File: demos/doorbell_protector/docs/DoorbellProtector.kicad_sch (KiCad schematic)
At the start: 15 parts

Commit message: export: kicad_sch — Phase 2.5b: layered placement, wire routing, KiCad 10 compatibility (#23)
* export: kicad_sch — Phase 2.5b: layered placement + routing + KiCad 9 fix

Placement (placement.py, complete rewrite):
- Replaces naive grid with Layered Signal Flow algorithm (spec §5 stages 1–8)
- Stage 1: band classification — power chips/rails at top, LEDs at bottom,
  everything else in the signal band
- Stage 2: signal-flow DAG via BFS from Rail/Connector sources; layer = BFS
  distance from nearest source
- Stage 3–4: place within (band, layer) cells at 1500-mil (38.1 mm) same-band
  spacing, 1000-mil inter-band gutter, 25.4 mm page margin
- Stage 6: cluster breakup — up to 10 iterations shifting same-band parts
  that land closer than 0.9× SAME_BAND_SPACING_MM
- Stage 8: page sized to fit (A4 → A3 → A2 → A1)
- grid_place() and sheet_size_mm() kept as shims for backward-compat

Routing (routing.py, new file):
- route_net(): connects stub ends with Manhattan L-shapes (horizontal first)
- find_junctions(): returns points where ≥3 wire endpoints coincide
- renderer uses routed wires between signal-net stub ends

Hierarchical (hierarchical.py, new file):
- collect_boards(), is_multi_board(), sub_sheet_filename() — interface stub
  for multi-Board sub-sheet emission (full implementation deferred)

KiCad 9 sub-symbol name fix (library_loader.py):
- KiCad 9 schematics expect sub-symbols nested inside their parent in
  lib_symbols to use the bare name (R_0_1, LED_0_1, 4069_1_0) — NOT the
  lib-qualified name (Device:R_0_1, Device:LED_0_1, 4xxx:4069_1_0)
- Fixed _qualify_names() to add the lib: prefix only to the exact parent
  symbol name using a lookahead (?=") that prevents sub-unit names from
  being qualified

Tests (+25 tests):
- test_placement.py: band classification, all-on-grid, determinism,
  minimum spacing, power < signal < indicator Y ordering, page sizing
- test_routing.py: H/V segments, L-shapes, orthogonality, grid snap,
  junction detection

Golden files re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
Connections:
- net Net-(Q2-b) is gone; now on net Net-(C4-t1): R4.1, R4.2
- net Net-(Q2-c) is gone; now on net Net-(C4-t1): R5.1, R5.2
- net Net-(C4-t1): now also C5.1, C5.2, R2.1, R2.2, R3.1, R3.2, R6.1, R6.2, R7.1, R7.2, R8.1, R8.2
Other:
- moved on the sheet: C1, C2, C3, C4, C5, D1, D2, R1, R2, R3, R4, R5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

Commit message: framework: passive + diode terminals mandatory (#30)
Continuation of the LED.cathode regression fix (#29). Resistor,
Capacitor, Inductor, and every Diode subclass had their terminals
declared `mandatory=False` with the same "structurally inert under
graph evaluation" justification — letting demos declare BOM-only
timing / decoupling / pull-up parts without wiring them, then ship
breadboard SVGs and netlists where those parts sat orphaned.

A real resistor / capacitor / inductor / diode with a dangling
terminal does nothing. Marking the ports mandatory closes the
silent regression at the framework layer.

  - `src/components/passives/{resistor,capacitor,inductor}.py` and
    every diode subclass under `src/components/diodes/` now declare
    their terminals `mandatory=True`.
  - `tests/components/test_{resistor,capacitor,inductor}.py`:
    regression tests pin the new contract per component.
  - `tests/components/test_diode_mandatory_terminals.py` (new):
    parametrized over D1N4001 / D1N4007 / D1N4148 / D1N4728A /
    D1N4733A / D1N4742A / D1N5817.
  - Six demos (`backup_power`, `bldc_motor`, `dice`,
    `doorbell_protector`, `fan_cooling`, `isolated_rs232`) had
    declared-but-unwired passives — each now wires them either to
    their datasheet-correct net (e.g. DoorbellProtector's flyback
    diode anode joins the relay coil_minus net) or as an isolated
    0-Ω passthrough with `dynamically_driven=True` where the part
    is genuinely BOM-only and the voltage-only simulator can't
    honour its behaviour. Comments at each call site explain
    which kind.
  - Test fixtures across CLI, refdes, format-roundtrip, kicad
    import, and per-format renderer tests updated so they still
    pin down the specific error each one exists to catch without
    tripping the new mandatory-pin check first.
  - All demo docs regenerated; goldens refreshed.

After this commit the breadboard SVGs show every BOM part connected
to something — no more orphaned caps and resistors float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
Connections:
- net Net-(C4-t1) is gone; now on net VCC: C4.1, C4.2, C5.1, C5.2, D2.1 (K), R1.1, R1.2, R2.1, R2.2, R3.1, R3.2, R4.1, R4.2, R5.1, R5.2, R6.1, R6.2, R7.1, R7.2, R8.1, R8.2
- net VCC: now also C1.1, C1.2, C2.1, C2.2, C3.1, C3.2

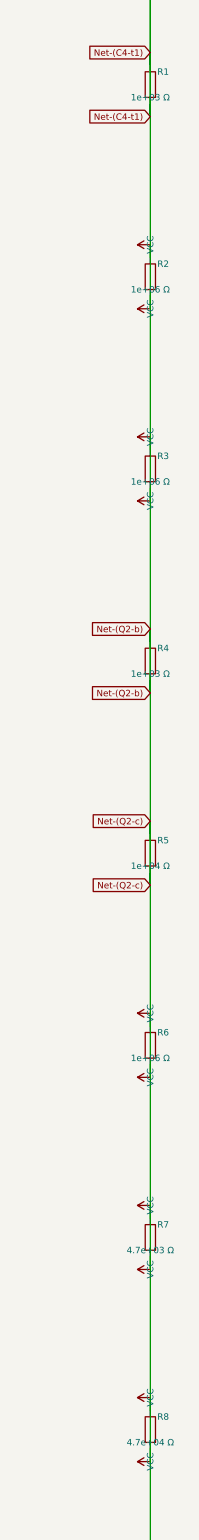
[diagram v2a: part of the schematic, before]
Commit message: units: Ohms.__str__ uses engineering notation (kΩ, MΩ, GΩ)
The previous `Ohms.__str__` formatted with bare `:.3g`, producing
unreadable scientific output for clean kilo / mega multiples:

  str(Ohms(10_000))     == "1e+04 Ω"      → now "10 kΩ"
  str(Ohms(100_000))    == "1e+05 Ω"      → now "100 kΩ"
  str(Ohms(1_000_000))  == "1e+06 Ω"      → now "1 MΩ"

The breadboard SVG visualiser surfaced the problem: a resistor body
labelled "100000Ω" makes a reader count zeros, while a label of
"100 kΩ" reads at a glance — exactly the convention every schematic
and parts catalogue uses. Centralising the engineering notation in
`Ohms.__str__` means every downstream consumer (assembly guide,
breadboard SVG, kicad netlist, BOM, reports) inherits the readable
form without each format adapter rolling its own formatter.

  - `Ohms.__str__` returns "47 Ω", "4.7 kΩ", "10 kΩ", "100 kΩ",
    "1 MΩ", "10 MΩ", "1 GΩ" per the kilo / mega / giga thresholds.
  - `Resistor.__str__` delegates to `str(self._ohms)` so it
    inherits the new notation (was producing the noisy "47.0 Ω"
    via raw float).
  - The breadboard visualiser's resistor body label uses
    `str(part.ohms)` directly (previously had a private
    `_format_ohms_compact` helper; removed).
  - `tests/components/test_resistor.py::test_str` updated for
    "47 Ω" (was "47.0 Ω"); new `test_str_renders_in_engineering_notation`
    pins kΩ / MΩ output across the kilo and mega thresholds.
  - All demo docs / goldens refreshed where the Ohms.__str__
    change affected the rendered output (breadboard SVGs, kicad
    sch value fields, BOM rows).
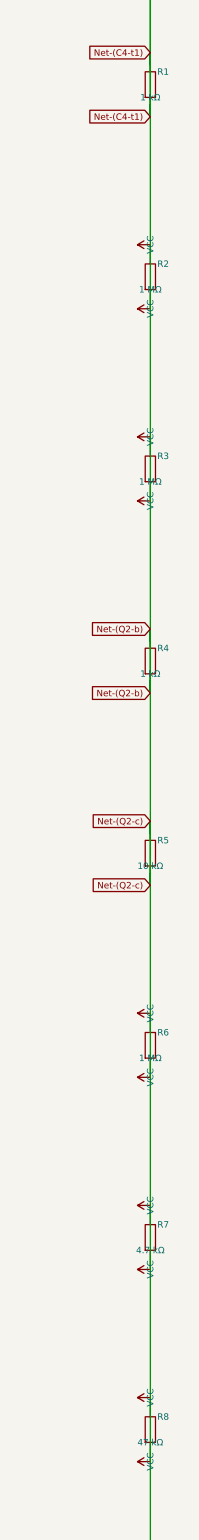
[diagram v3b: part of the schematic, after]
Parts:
- R1, R4: value 1e+03 Ω -> 1 kΩ
- R2, R3, R6: value 1e+06 Ω -> 1 MΩ
- R5: value 1e+04 Ω -> 10 kΩ
- R7: value 4.7e+03 Ω -> 4.7 kΩ
- R8: value 4.7e+04 Ω -> 47 kΩ
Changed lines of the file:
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@@
       (effects (font (size 1.27 1.27)))
     )
-    (property "Value" "1e+03 Ω"
+    (property "Value" "1 kΩ"
       (at 63.5 485.14 0)
       (effects (font (size 1.27 1.27)))
@@
       (effects (font (size 1.27 1.27)))
     )
-    (property "Value" "1e+06 Ω"
+    (property "Value" "1 MΩ"
       (at 63.5 523.24 0)
       (effects (font (size 1.27 1.27)))
@@
       (effects (font (size 1.27 1.27)))
     )
-    (property "Value" "1e+06 Ω"
+    (property "Value" "1 MΩ"
       (at 63.5 561.34 0)
       (effects (font (size 1.27 1.27)))
@@
       (effects (font (size 1.27 1.27)))
     )
-    (property "Value" "1e+03 Ω"
+    (property "Value" "1 kΩ"
       (at 63.5 599.44 0)
       (effects (font (size 1.27 1.27)))
@@
       (effects (font (size 1.27 1.27)))
     )
-    (property "Value" "1e+04 Ω"
+    (property "Value" "10 kΩ"
       (at 63.5 637.54 0)
       (effects (font (size 1.27 1.27)))
@@
       (effects (font (size 1.27 1.27)))
     )
-    (property "Value" "1e+06 Ω"
+    (property "Value" "1 MΩ"
       (at 63.5 675.64 0)
       (effects (font (size 1.27 1.27)))
@@
       (effects (font (size 1.27 1.27)))
     )
-    (property "Value" "4.7e+03 Ω"
+    (property "Value" "4.7 kΩ"
       (at 63.5 713.74 0)
       (effects (font (size 1.27 1.27)))
@@
       (effects (font (size 1.27 1.27)))
     )
-    (property "Value" "4.7e+04 Ω"
+    (property "Value" "47 kΩ"
       (at 63.5 751.84 0)
       (effects (font (size 1.27 1.27)))

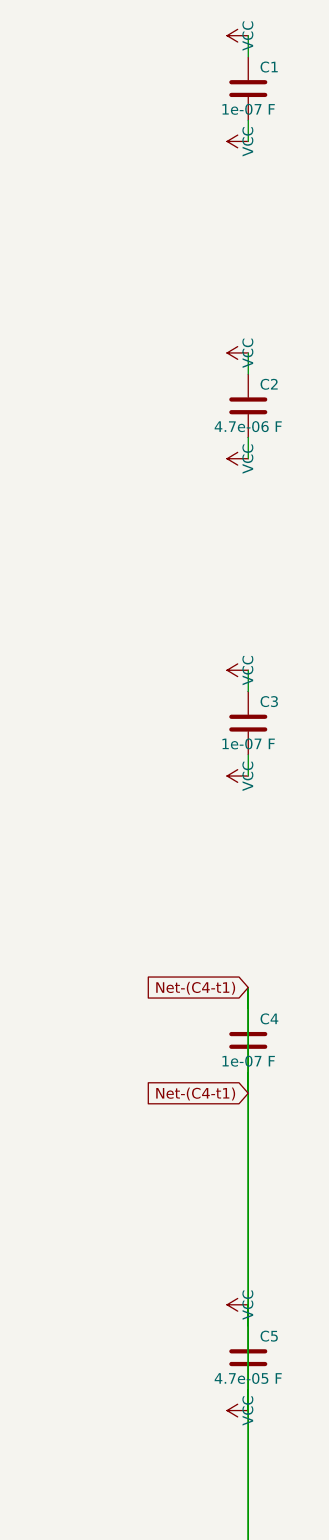
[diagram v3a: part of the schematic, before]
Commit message: units: Farads + Henries __str__ also use engineering notation
Same treatment as `Ohms.__str__` (previous commit) for the other two
passive engineering quantities. Demos contain caps and inductors
with values that the bare `:.3g` formatter would emit in scientific
form (`1e-07 F` for a 100 nF decoupling cap); centralising the
engineering notation on the unit class means every consumer
(reports, BOM, breadboard SVG, etc.) inherits the readable form.

  - `Farads.__str__` returns `100 pF`, `22 nF`, `100 nF`, `1 µF`,
    `4.7 µF`, `470 µF`, `1 mF`, `1 F` across the standard
    capacitance bands.
  - `Henries.__str__` returns `100 nH`, `10 µH`, `22 mH`, `1 H`
    across the standard inductance bands.
  - `Capacitor.__str__` and `Inductor.__str__` delegate to the
    unit class's str (were rolling raw-float formatters).
  - `framework.export.reports_common.part_description` now uses
    `str(part.ohms / farads / henries)` directly instead of the
    parallel `_format_ohms` / `_format_farads` / `_format_henries`
    helpers (removed — they duplicated the new logic on raw
    floats).
  - Breadboard SVG renderer now also labels capacitor and inductor
    bodies with their engineering-notation value (was only
    resistors).
  - `tests/framework/test_units.py`: parametrised regression tests
    for both unit classes across every band.
  - All affected demo docs / goldens refreshed.
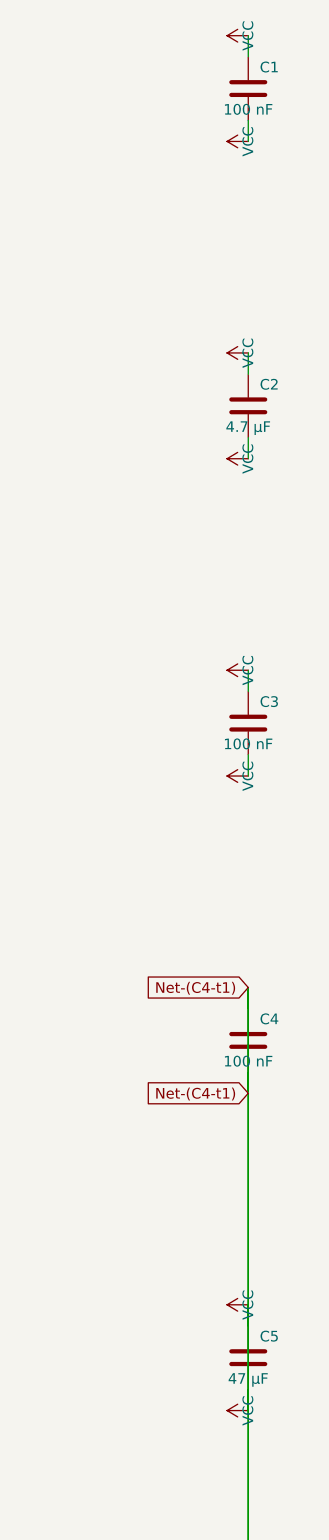
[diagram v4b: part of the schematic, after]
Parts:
- C1, C3, C4: value 1e-07 F -> 100 nF
- C2: value 4.7e-06 F -> 4.7 µF
- C5: value 4.7e-05 F -> 47 µF
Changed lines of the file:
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@@
       (effects (font (size 1.27 1.27)))
     )
-    (property "Value" "1e-07 F"
+    (property "Value" "100 nF"
       (at 63.5 27.94 0)
       (effects (font (size 1.27 1.27)))
@@
       (effects (font (size 1.27 1.27)))
     )
-    (property "Value" "4.7e-06 F"
+    (property "Value" "4.7 µF"
       (at 63.5 66.04 0)
       (effects (font (size 1.27 1.27)))
@@
       (effects (font (size 1.27 1.27)))
     )
-    (property "Value" "1e-07 F"
+    (property "Value" "100 nF"
       (at 63.5 104.14 0)
       (effects (font (size 1.27 1.27)))
@@
       (effects (font (size 1.27 1.27)))
     )
-    (property "Value" "1e-07 F"
+    (property "Value" "100 nF"
       (at 63.5 142.24 0)
       (effects (font (size 1.27 1.27)))
@@
       (effects (font (size 1.27 1.27)))
     )
-    (property "Value" "4.7e-05 F"
+    (property "Value" "47 µF"
       (at 63.5 180.34 0)
       (effects (font (size 1.27 1.27)))
